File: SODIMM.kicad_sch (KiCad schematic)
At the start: 5 parts, among them CN1 YXT-BB10-50P-02, CN2 YXT-BB10-50P-02, CN3 YXT-BB10-50P-02, U6 Compute_Module_4_Connectors, U7 Compute_Module_4_Functional

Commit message: changed some ethernet stuff
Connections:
- net GND: now also CN2.12, CN2.16, CN2.3, CN2.6, CN2.9, CN3.10, CN3.14, CN3.17, CN3.45, CN3.5
- net ENET_MDI0+: now reaches CN2.1
- net ENET_MDI3+: now reaches CN2.10
- net ENET_MDI3-: now reaches CN2.11
- net ENET_LED1: now reaches CN2.13
- net ENET_LED0: now reaches CN2.14
- net ENET_LED2: now reaches CN2.15
- net ENET_MDI0-: now reaches CN2.2
- net ENET_MDI1+: now reaches CN2.4
- net ENET_MDI1-: now reaches CN2.5
- net ENET_MDI2+: now reaches CN2.7
- net ENET_MDI2-: now reaches CN2.8
- net JTAG_MS: now reaches CN3.1
- net PA8: now reaches CN3.11
- net PA9: now reaches CN3.12
- net PA10: now reaches CN3.13
- net TWI0_SCK: now reaches CN3.15
- net TWI0_SDA: now reaches CN3.16
- net UART3_TX: now reaches CN3.18
- net UART3_RX: now reaches CN3.19
- net JTAG_CK: now reaches CN3.2
- net UART3_RTS: now reaches CN3.20
- net UART3_CTS: now reaches CN3.21
- net JTAG_DO: now reaches CN3.3
- net JTAG_DI: now reaches CN3.4
- net SPI0_CS: now reaches CN3.41
- net SPI0_CLK: now reaches CN3.42
- net SPI0_MISO: now reaches CN3.43
- net SPI0_MOSI: now reaches CN3.44
- net PA21: now reaches CN3.46
- net PA20: now reaches CN3.47
- net PA19: now reaches CN3.48
- net PA18: now reaches CN3.49
- net PA17: now reaches CN3.50
- net PA4: now reaches CN3.6
- net PA5: now reaches CN3.7
- net PA6: now reaches CN3.8
- net PA7: now reaches CN3.9
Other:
- note added: "Connections for - Power \, USB (0-3) \, HDMI \. Ethernet \, SD \, Audio \, IO \, JTAG"
- note removed: "Connections for - Power \, USB (0-3) \, HDMI - Ethernet \, SD - Audio"
- moved on the sheet: CN2, CN3, U7B, U7D, U7E, U7F, U7G, U7I, U7J

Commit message: power changes
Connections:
- net GND: now also CN1.28
- net CHG_LED: now reaches CN1.26
- net PWR_ON: now reaches CN1.27
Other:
- moved on the sheet: CN1

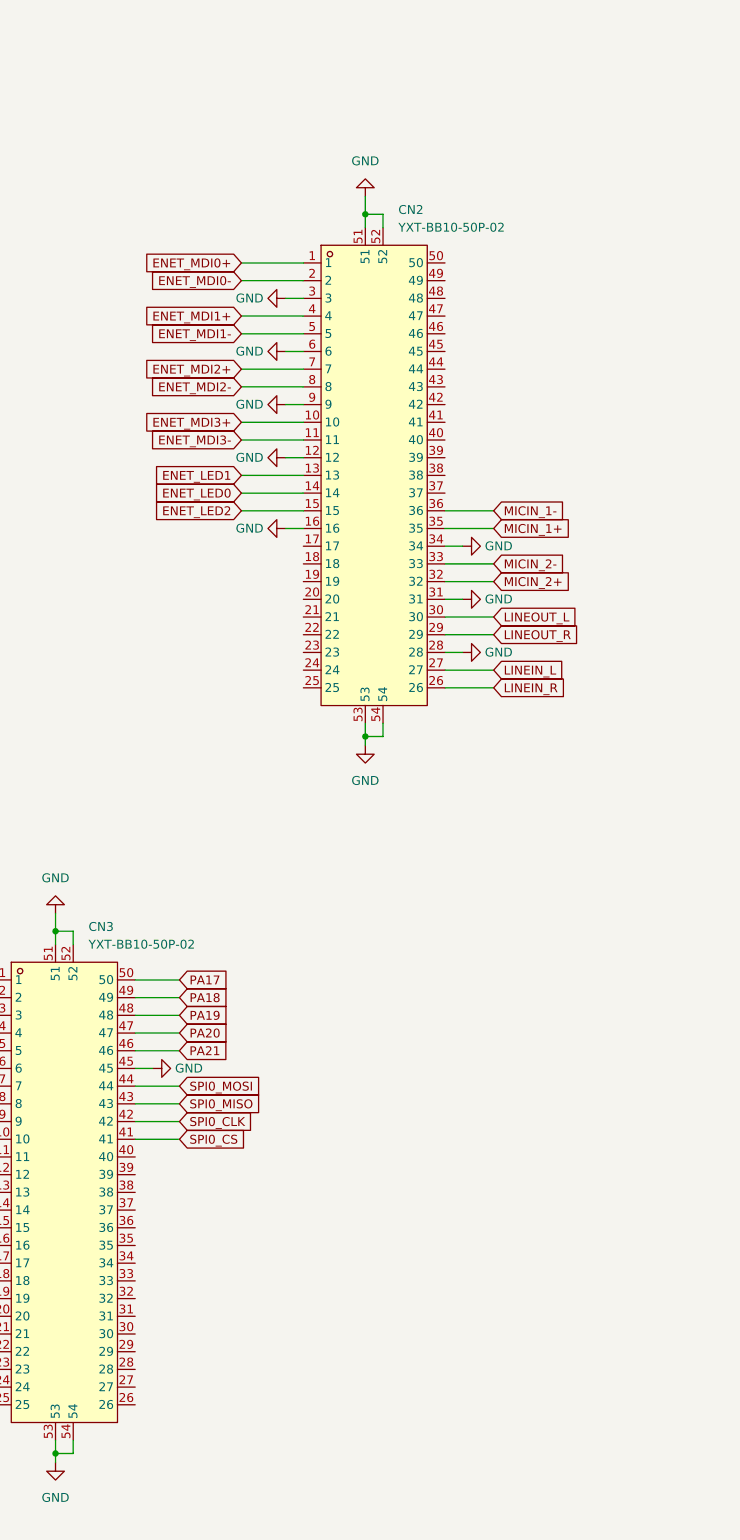
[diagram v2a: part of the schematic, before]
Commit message: power changes and pinout update
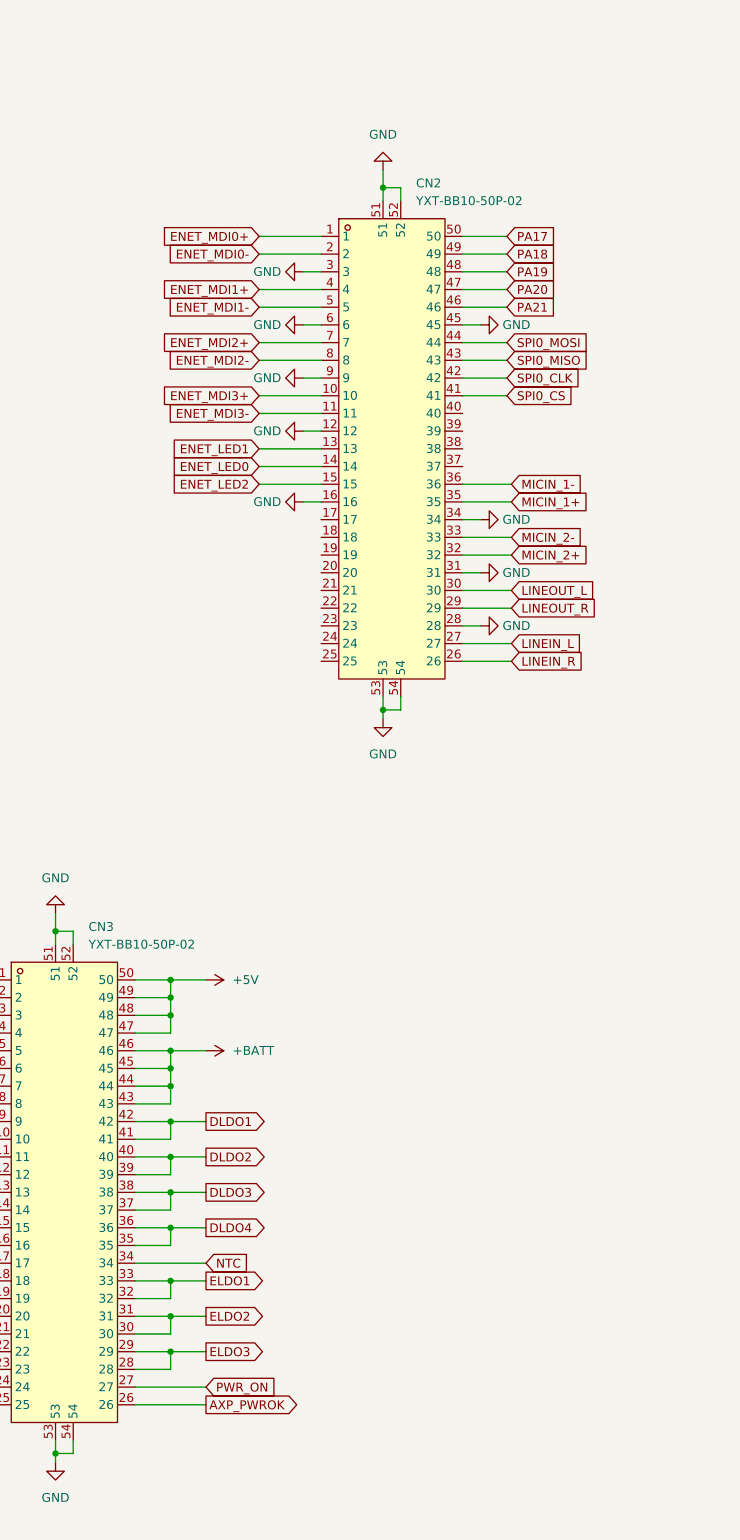
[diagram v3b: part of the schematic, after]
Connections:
- net GND: now also CN2.45; no longer CN3.45
- net PA17: now also CN2.50; no longer CN3.50
- net PA18: now also CN2.49; no longer CN3.49
- net PA19: now also CN2.48; no longer CN3.48
- net PA20: now also CN2.47; no longer CN3.47
- net PA21: now also CN2.46; no longer CN3.46
- net PWR_ON: now also CN3.27
- net SPI0_CLK: now also CN2.42; no longer CN3.42
- net SPI0_CS: now also CN2.41; no longer CN3.41
- net SPI0_MISO: now also CN2.43; no longer CN3.43
- net SPI0_MOSI: now also CN2.44; no longer CN3.44
- net AXP_PWROK: now reaches CN3.26
- net ELDO3: now reaches CN3.28
- net ELDO3: now also CN3.29
- net ELDO2: now reaches CN3.30
- net ELDO2: now also CN3.31
- net ELDO1: now reaches CN3.32
- net ELDO1: now also CN3.33
- net NTC: now reaches CN3.34
- net DLDO4: now reaches CN3.35
- net DLDO4: now also CN3.36
- net DLDO3: now reaches CN3.37
- net DLDO3: now also CN3.38
- net DLDO2: now reaches CN3.39
- net DLDO2: now also CN3.40
- new net +5V: CN3.47, CN3.48, CN3.49, CN3.50
- new net +BATT: CN3.43, CN3.44, CN3.45, CN3.46
- new net DLDO1: CN3.41, CN3.42
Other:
- moved on the sheet: CN2

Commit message: power things, minor changes
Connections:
- net UBOOT: now reaches CN2.17
- net DCDC4: now reaches CN2.22
- net DCDC4: now also CN2.23, CN2.24, CN2.25
- net TVOUT: now reaches CN3.23

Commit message: small changes
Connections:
- net GND: now also CN2.18, CN2.21, CN2.37, CN2.40, CN3.22, CN3.24, CN3.25
- net PG0: now reaches CN1.18
- net PG1: now reaches CN1.19
- net PG2: now reaches CN1.20
- net PG3: now reaches CN1.21
- net PG4: now reaches CN1.22
- net PG5: now reaches CN1.23
- net PG6: now reaches CN1.24
- net PG7: now reaches CN1.25
- net PG8: now reaches CN2.19
- net PG9: now reaches CN2.20
- net PG11: now reaches CN2.38
- net PG10: now reaches CN2.39

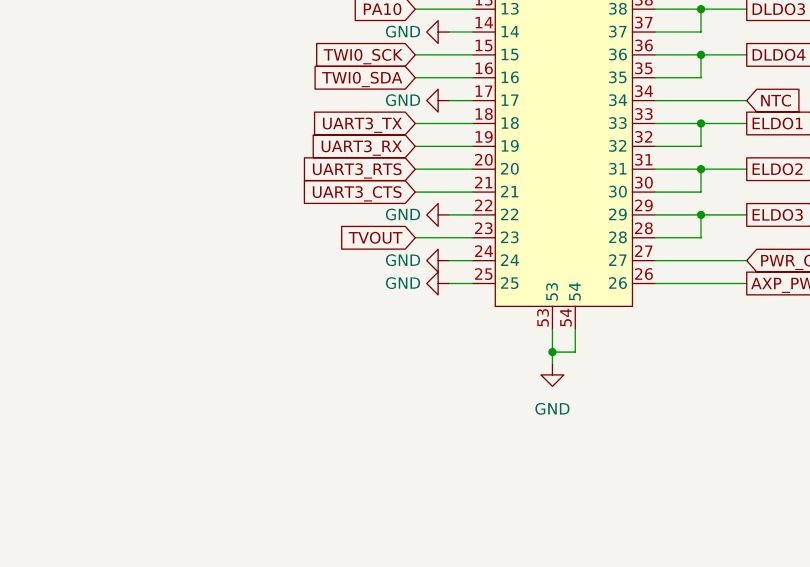
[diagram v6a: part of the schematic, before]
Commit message: recovered ethernet power changes
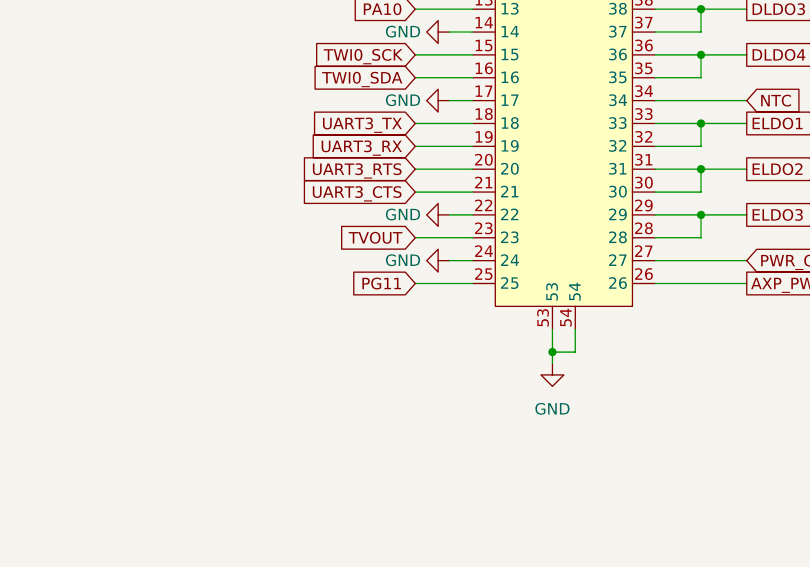
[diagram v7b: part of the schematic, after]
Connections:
- net GND: no longer CN3.25
- net PG11: now also CN3.25
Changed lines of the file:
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@@
 	(wire
 		(pts
-			(xy 133.35 246.38) (xy 135.89 246.38)
-		)
-		(stroke
-			(width 0)
-			(type default)
-		)
-	)
-	(wire
-		(pts
 			(xy 156.21 198.12) (xy 161.29 198.12)
 		)
@@
 	(wire
 		(pts
+			(xy 129.54 246.38) (xy 135.89 246.38)
+		)
+		(stroke
+			(width 0)
+			(type default)
+		)
+	)
+	(wire
+		(pts
 			(xy 182.88 93.98) (xy 173.99 93.98)
 		)
@@
 		)
 	)
+	(global_label "PG11"
+		(shape input)
+		(at 129.54 246.38 180)
+		(fields_autoplaced yes)
+		(effects
+			(font
+				(size 1.27 1.27)
+			)
+			(justify right)
+		)
+		(property "Intersheetrefs" "${INTERSHEET_REFS}"
+			(at 121.5958 246.38 0)
+			(effects
+				(font
+					(size 1.27 1.27)
+				)
+				(justify right)
+				(hide yes)
+			)
+		)
+	)
 	(global_label "USB1_D+"
 		(shape input)
@@
 					(unit 1)
 				)
-			)
-		)
-	)
-	(symbol
-		(lib_id "power:GND")
-		(at 133.35 246.38 270)
-		(unit 1)
-		(exclude_from_sim no)
-		(in_bom yes)
-		(on_board yes)
-		(dnp no)
-		(fields_autoplaced yes)
-		(property "Reference" "#PWR078"
-			(at 127 246.38 0)
-			(effects
-				(font
-					(size 1.27 1.27)
-				)
-				(hide yes)
-			)
-		)
-		(property "Value" "GND"
-			(at 130.175 246.38 90)
-			(effects
-				(font
-					(size 1.27 1.27)
-				)
-				(justify right)
-			)
-		)
-		(property "Footprint" ""
-			(at 133.35 246.38 0)
-			(effects
-				(font
-					(size 1.27 1.27)
-				)
-				(hide yes)
-			)
-		)
-		(property "Datasheet" ""
-			(at 133.35 246.38 0)
-			(effects
-				(font
-					(size 1.27 1.27)
-				)
-				(hide yes)
-			)
-		)
-		(property "Description" ""
-			(at 133.35 246.38 0)
-			(effects
-				(font
-					(size 1.27 1.27)
-				)
-			)
-		)
-		(pin "1"
-		)
-		(instances
-			(project "H3_SBC"
-				(path "/2511caf5-b791-49bc-bcf7-734707cf883b/820235b6-3e55-4f19-988b-04cbfedf3fbe"
-					(reference "#PWR078")
-					(unit 1)
-				)

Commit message: linking symbols to footprints
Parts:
- removed U6: Compute_Module_4_Connectors, symbol Raspberry_Pi_Compute_Module_4:Compute_Module_4_Connectors
- removed U7: Compute_Module_4_Functional, symbol Raspberry_Pi_Compute_Module_4:Compute_Module_4_Functional
